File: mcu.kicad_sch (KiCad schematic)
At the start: 21 parts, among them J1 AVR ISP, J2 PRG/BL0942, Q1 2N7002, U6 ATmega328PB-A, U7 AT25xxx

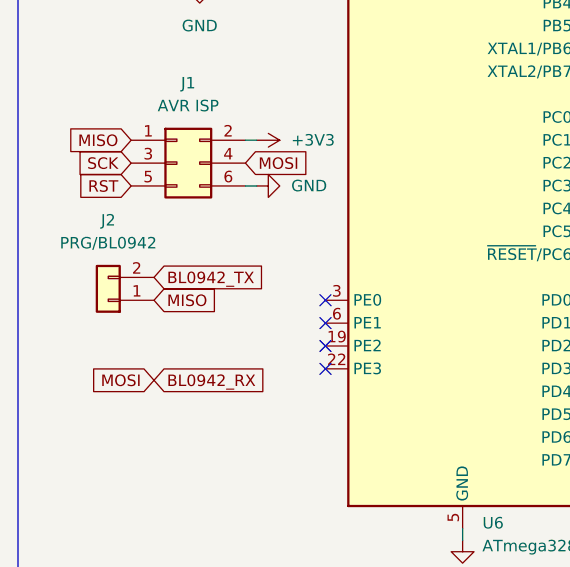
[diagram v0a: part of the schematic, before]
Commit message: remove BL0942 TX pin jumper and add pull up resistor
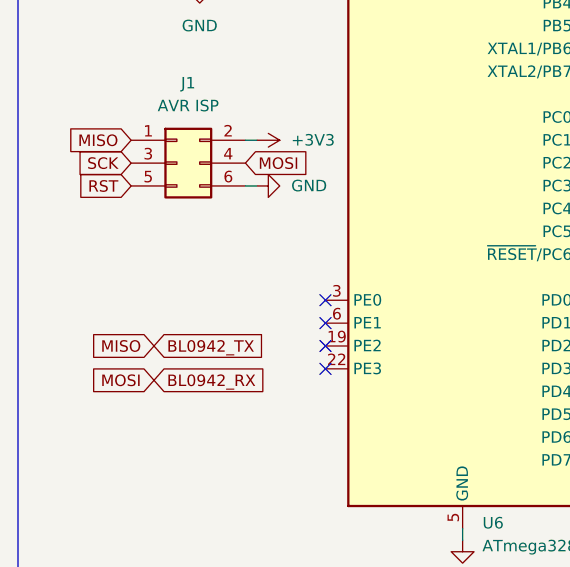
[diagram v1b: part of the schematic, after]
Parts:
- removed J2: PRG/BL0942, Connector_PinHeader_2.54mm:PinHeader_1x02_P2.54mm_Vertical, symbol Connector_Generic:Conn_01x02
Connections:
- net MISO is gone; now on net BL0942_TX: J1.1 (Pin_1), U6.16 (PB4), U7.2 (MISO)
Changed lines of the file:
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@@
 	(global_label "BL0942_TX"
 		(shape input)
-		(at 62.23 87.63 0)
-		(fields_autoplaced yes)
-		(effects
-			(font
-				(size 1.27 1.27)
-			)
-			(justify left)
-		)
-		(property "Intersheetrefs" "${INTERSHEET_REFS}"
-			(at 75.496 87.63 0)
+		(at 62.23 95.25 0)
+		(fields_autoplaced yes)
+		(effects
+			(font
+				(size 1.27 1.27)
+			)
+			(justify left)
+		)
+		(property "Intersheetrefs" "${INTERSHEET_REFS}"
+			(at 75.496 95.25 0)
 			(effects
 				(font
@@
 	(global_label "MISO"
 		(shape input)
-		(at 62.23 90.17 0)
-		(fields_autoplaced yes)
-		(effects
-			(font
-				(size 1.27 1.27)
-			)
-			(justify left)
-		)
-		(property "Intersheetrefs" "${INTERSHEET_REFS}"
-			(at 69.8114 90.17 0)
-			(effects
-				(font
-					(size 1.27 1.27)
-				)
-				(justify left)
+		(at 62.23 95.25 180)
+		(fields_autoplaced yes)
+		(effects
+			(font
+				(size 1.27 1.27)
+			)
+			(justify right)
+		)
+		(property "Intersheetrefs" "${INTERSHEET_REFS}"
+			(at 54.6486 95.25 0)
+			(effects
+				(font
+					(size 1.27 1.27)
+				)
+				(justify right)
 				(hide yes)
 			)
@@
 					(unit 1)
 				)
-			)
-		)
-	)
-	(symbol
-		(lib_id "Connector_Generic:Conn_01x02")
-		(at 57.15 90.17 180)
-		(unit 1)
-		(exclude_from_sim no)
-		(in_bom yes)
-		(on_board yes)
-		(dnp no)
-		(fields_autoplaced yes)
-		(property "Reference" "J2"
-			(at 57.15 81.28 0)
-			(effects
-				(font
-					(size 1.27 1.27)
-				)
-			)
-		)
-		(property "Value" "PRG/BL0942"
-			(at 57.15 83.82 0)
-			(effects
-				(font
-					(size 1.27 1.27)
-				)
-			)
-		)
-		(property "Footprint" "Connector_PinHeader_2.54mm:PinHeader_1x02_P2.54mm_Vertical"
-			(at 57.15 90.17 0)
-			(effects
-				(font
-					(size 1.27 1.27)
-				)
-				(hide yes)
-			)
-		)
-		(property "Datasheet" "~"
-			(at 57.15 90.17 0)
-			(effects
-				(font
-					(size 1.27 1.27)
-				)
-				(hide yes)
-			)
-		)
-		(property "Description" "Generic connector, single row, 01x02, script generated (kicad-library-utils/schlib/autogen/connector/)"
-			(at 57.15 90.17 0)
-			(effects
-				(font
-					(size 1.27 1.27)
-				)
-				(hide yes)
-			)
-		)
-		(pin "1"
-		)
-		(pin "2"
-		)
-		(instances
-			(project ""
-				(path "/73ae532b-17b2-4152-9abe-0d6b33529f07/fd4e76ca-d530-44c8-b4ec-e44050bd29b3"
-					(reference "J2")
-					(unit 1)
-				)

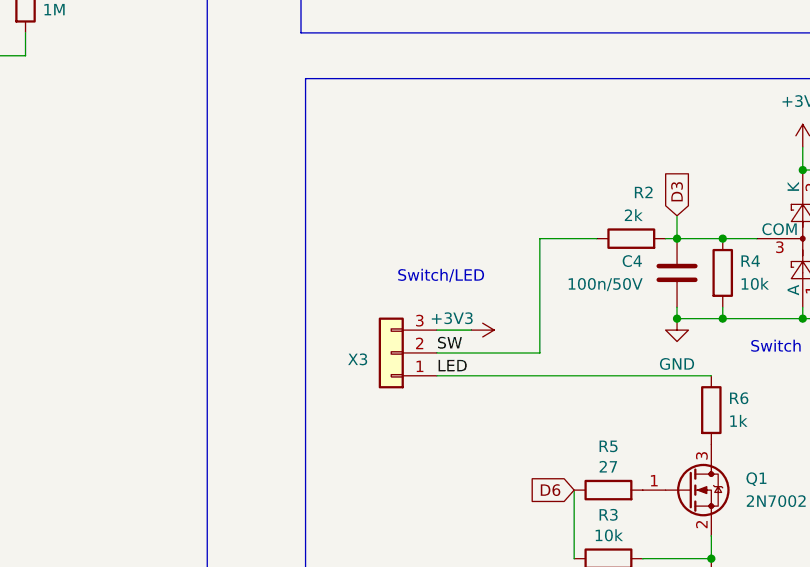
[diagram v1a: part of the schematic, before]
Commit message: add BOM + update schematic parts descriptions
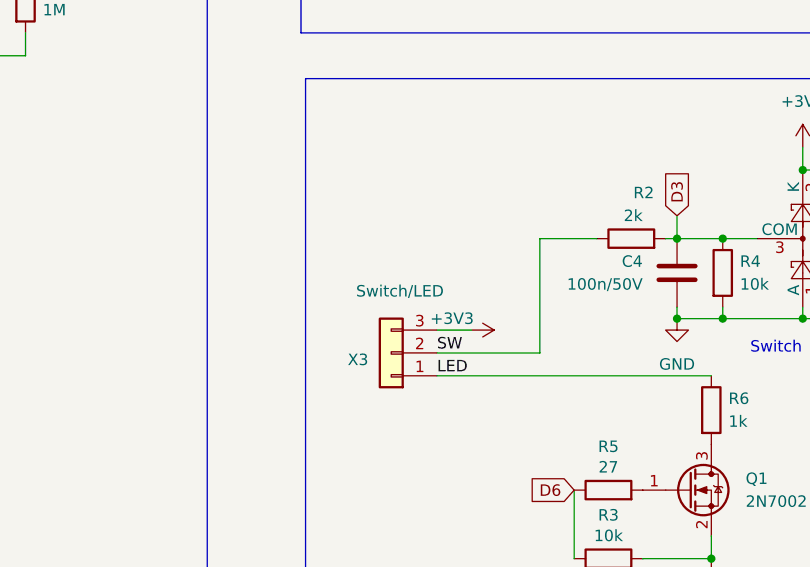
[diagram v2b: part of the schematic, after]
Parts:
- X3: value ~ -> Switch/LED
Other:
- note removed: "Switch/LED"
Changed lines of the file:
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@@
-		)
-	)
-	(text "Switch/LED"
-		(exclude_from_sim no)
-		(at 183.134 110.49 0)
-		(effects
-			(font
-				(size 1.27 1.27)
-			)
-			(justify right bottom)
 		)
 	)
@@
 			)
 		)
-		(property "Value" "~"
-			(at 169.545 116.84 0)
-			(effects
-				(font
+		(property "Value" "Switch/LED"
+			(at 178.562 111.252 0)
+			(effects
+				(font
